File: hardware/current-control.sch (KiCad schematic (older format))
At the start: 9 parts, among them J201 Conn_01x01_Male, Q201 BTS141, U102 TLV4333, U201 DAC6571

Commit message: After footprint check, before layout
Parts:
- added R201, R206: 10K, Resistor_SMD:R_0805_2012Metric_Pad1.15x1.40mm_HandSolder, symbol Device:R
- added R207: 22K, Resistor_SMD:R_0805_2012Metric_Pad1.15x1.40mm_HandSolder, symbol Device:R
- added R208: 220K, Resistor_SMD:R_0805_2012Metric_Pad1.15x1.40mm_HandSolder, symbol Device:R
- C201: MPN (none) -> 885012207098
- J201: MPN (none) -> RA-T2X-64E
- R202: renamed from R201; value 23K -> 220K; MPN (none) -> CRGP0805F220K
- R203: renamed from R202; value 10K -> 22K; MPN (none) -> CRGP0805F22K
- R204: renamed from R203; MPN (none) -> CRGP0805F1K0
- R205: renamed from R204; value 0.1, 1W -> 10m, 3W; MPN SR3R1000FE66 -> RMCJ2U00R01FS
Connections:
- net GND: now also R201.2, R206.2, R207.2
- net I_SENSE: now also R208.1; no longer U102.6 (-)
- net at R202.2, R203.1, U102.3 (+): now also R201.1
- new net: R206.1, R207.1, R208.2, U102.6 (-)
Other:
- note added: "0-0.1V"
- note added: "0.01Ω sense resistor => 1A current / 10mV of programming voltage\n\nSo max. programming voltage of 0.1V =>max. current 10A\n\nBTS141 max. I_D = 25 A\n\nI = 10A, R = 0.01Ω => Power = I^2 R = 1W\nUse 3W sense resistor to give margin"
- note added: "Amplification of 33 here gives full range\nADC input for sense voltage range of 0-0.1V."
- note removed: "0-1V"
- note removed: "0.1Ω sense resistor => 1A current / 100mV of programming voltage\n\nSo max. programming voltage of 1V =>max. current 10A\n\nBTS141 max. I_D = 25 A"
- moved on the sheet: R203
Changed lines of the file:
@@
 L Device:R R?
 U 1 1 5E5F12A4
-P 5100 3625
+P 5175 3625
 AR Path="/5E5F12A4" Ref="R?"  Part="1"
-AR Path="/5E5EBC79/5E5F12A4" Ref="R202"  Part="1"
-F 0 "R202" H 5170 3671 50  0000 L CNN
-F 1 "10K" H 5170 3580 50  0000 L CNN
-F 2 "Resistor_SMD:R_0805_2012Metric_Pad1.15x1.40mm_HandSolder" V 5030 3625 50  0001 C CNN
-F 3 "~" H 5100 3625 50  0001 C CNN
-	1    5100 3625
+AR Path="/5E5EBC79/5E5F12A4" Ref="R203"  Part="1"
+F 0 "R203" H 5245 3671 50  0000 L CNN
+F 1 "22K" H 5245 3580 50  0000 L CNN
+F 2 "Resistor_SMD:R_0805_2012Metric_Pad1.15x1.40mm_HandSolder" V 5105 3625 50  0001 C CNN
+F 3 "https://www.mouser.at/datasheet/2/418/NG_DS_9-1773463-9_A-1358566.pdf" H 5175 3625 50  0001 C CNN
+F 4 "CRGP0805F22K" H 5175 3625 50  0001 C CNN "MPN"
+	1    5175 3625
 	1    0    0    -1
 $EndComp
@@
 P 7025 4100
 AR Path="/5E5F12B6" Ref="R?"  Part="1"
-AR Path="/5E5EBC79/5E5F12B6" Ref="R204"  Part="1"
-F 0 "R204" H 7095 4146 50  0000 L CNN
-F 1 "0.1, 1W" H 7095 4055 50  0000 L CNN
+AR Path="/5E5EBC79/5E5F12B6" Ref="R205"  Part="1"
+F 0 "R205" H 7095 4146 50  0000 L CNN
+F 1 "10m, 3W" H 7095 4055 50  0000 L CNN
 F 2 "teensy-load:Sense_Resistor" V 6955 4100 50  0001 C CNN
-F 3 "https://www.mouser.at/datasheet/2/427/sr-1762146.pdf" H 7025 4100 50  0001 C CNN
-F 4 "SR3R1000FE66" H 7025 4100 50  0001 C CNN "MPN"
+F 3 "https://www.mouser.at/datasheet/2/611/rmc-series-1074317.pdf" H 7025 4100 50  0001 C CNN
+F 4 "RMCJ2U00R01FS" H 7025 4100 50  0001 C CNN "MPN"
 	1    7025 4100
 	1    0    0    -1
@@
 P 6450 3450
 AR Path="/5E5F12DB" Ref="R?"  Part="1"
-AR Path="/5E5EBC79/5E5F12DB" Ref="R203"  Part="1"
-F 0 "R203" V 6243 3450 50  0000 C CNN
+AR Path="/5E5EBC79/5E5F12DB" Ref="R204"  Part="1"
+F 0 "R204" V 6243 3450 50  0000 C CNN
 F 1 "1K" V 6334 3450 50  0000 C CNN
 F 2 "Resistor_SMD:R_0805_2012Metric_Pad1.15x1.40mm_HandSolder" V 6380 3450 50  0001 C CNN
-F 3 "~" H 6450 3450 50  0001 C CNN
+F 3 "https://www.mouser.at/datasheet/2/418/NG_DS_9-1773463-9_A-1358566.pdf" H 6450 3450 50  0001 C CNN
+F 4 "CRGP0805F1K0" H 6450 3450 50  0001 C CNN "MPN"
 	1    6450 3450
 	0    1    1    0
@@
 Text HLabel 8650 2700 2    50   Input ~ 0
 IN+
-Text HLabel 8650 4475 2    50   Input ~ 0
+Text HLabel 8650 5275 2    50   Input ~ 0
 IN-
-Text Notes 6825 5000 0    50   ~ 0
-0.1Ω sense resistor => 1A current / 100mV of programming voltage\n\nSo max. programming voltage of 1V =>max. current 10A\n\nBTS141 max. I_D = 25 A
+Text Notes 6775 6200 0    50   ~ 0
+0.01Ω sense resistor => 1A current / 10mV of programming voltage\n\nSo max. programming voltage of 0.1V =>max. current 10A\n\nBTS141 max. I_D = 25 A\n\nI = 10A, R = 0.01Ω => Power = I^2 R = 1W\nUse 3W sense resistor to give margin
 Text HLabel 3225 2475 0    50   Input ~ 0
 I2C_SCL
@@
 P 5100 3025
 AR Path="/5E61CCF9" Ref="R?"  Part="1"
-AR Path="/5E5EBC79/5E61CCF9" Ref="R201"  Part="1"
-F 0 "R201" H 5170 3071 50  0000 L CNN
-F 1 "23K" H 5170 2980 50  0000 L CNN
+AR Path="/5E5EBC79/5E61CCF9" Ref="R202"  Part="1"
+F 0 "R202" H 5170 3071 50  0000 L CNN
+F 1 "220K" H 5170 2980 50  0000 L CNN
 F 2 "Resistor_SMD:R_0805_2012Metric_Pad1.15x1.40mm_HandSolder" V 5030 3025 50  0001 C CNN
-F 3 "~" H 5100 3025 50  0001 C CNN
+F 3 "https://www.mouser.at/datasheet/2/418/NG_DS_9-1773463-9_A-1358566.pdf" H 5100 3025 50  0001 C CNN
+F 4 "CRGP0805F220K" H 5100 3025 50  0001 C CNN "MPN"
 	1    5100 3025
 	1    0    0    -1
@@
 Wire Wire Line
 	5625 3350 5100 3350
-Connection ~ 5100 3350
-Wire Wire Line
-	5100 3350 5100 3475
 Wire Wire Line
 	5100 2875 5100 2625
@@
 	5100 2625 4625 2625
 Wire Wire Line
-	7025 4250 7025 4475
-Wire Wire Line
-	7025 4475 8650 4475
+	7025 5275 8650 5275
 Wire Wire Line
 	7025 3650 7025 3825
@@
 	5500 3825 7025 3825
 Connection ~ 7025 3825
-Wire Wire Line
-	5100 3775 5100 3900
 Text Notes 4825 2600 0    50   ~ 0
 0-3.3V
 Text Notes 5200 3325 0    50   ~ 0
-0-1V
+0-0.1V
 Wire Wire Line
 	4175 3900 5100 3900
 Wire Wire Line
 	4175 3100 4175 3900
-Connection ~ 5100 3900
 Wire Wire Line
 	5100 3900 5100 4000
@@
 F 1 "0.1U" H 2165 2455 50  0000 L CNN
 F 2 "Capacitor_SMD:C_0805_2012Metric_Pad1.15x1.40mm_HandSolder" H 2088 2350 50  0001 C CNN
-F 3 "~" H 2050 2500 50  0001 C CNN
+F 3 "https://www.mouser.at/datasheet/2/445/885012207098-1727748.pdf" H 2050 2500 50  0001 C CNN
+F 4 "885012207098" H 2050 2500 50  0001 C CNN "MPN"
 	1    2050 2500
 	1    0    0    -1
@@
 Wire Wire Line
 	8300 4000 8375 4000
-Wire Wire Line
-	8375 4000 8375 4300
-Wire Wire Line
-	8375 4300 7600 4300
-Wire Wire Line
-	7600 4300 7600 4100
 Wire Wire Line
 	7600 4100 7700 4100
@@
 F 1 "Conn_01x01_Male" H 7808 3265 50  0000 C CNN
 F 2 "teensy-load:HeatSink_RA_T2X_64E" H 7700 3175 50  0001 C CNN
-F 3 "~" H 7700 3175 50  0001 C CNN
+F 3 "https://www.ohmite.com/assets/docs/sink_f_r.pdf" H 7700 3175 50  0001 C CNN
+F 4 "RA-T2X-64E" H 7700 3175 50  0001 C CNN "MPN"
 	1    7700 3175
 	1    0    0    -1
@@
 Text Notes 7625 3300 0    50   ~ 0
 Heat sink
+Text Notes 7825 5000 0    50   ~ 0
+Amplification of 33 here gives full range\nADC input for sense voltage range of 0-0.1V.
+$Comp
+L Device:R R208
+U 1 1 5E7C1E35
+P 8075 4400
+F 0 "R208" V 8175 4400 50  0000 C CNN
+F 1 "220K" V 8275 4400 50  0000 C CNN
+F 2 "Resistor_SMD:R_0805_2012Metric_Pad1.15x1.40mm_HandSolder" V 8005 4400 50  0001 C CNN
+F 3 "https://www.mouser.at/datasheet/2/418/NG_DS_9-1773463-9_A-1358566.pdf" H 8075 4400 50  0001 C CNN
+F 4 "CRGP0805F220K" H 8075 4400 50  0001 C CNN "MPN"
+	1    8075 4400
+	0    1    1    0
+$EndComp
+Wire Wire Line
+	7600 4100 7600 4400
+Wire Wire Line
+	8375 4000 8375 4400
+$Comp
+L power:GND #PWR?
+U 1 1 5E7C4D35
+P 7600 4950
+AR Path="/5E7C4D35" Ref="#PWR?"  Part="1"
+AR Path="/5E5EBC79/5E7C4D35" Ref="#PWR0205"  Part="1"
+F 0 "#PWR0205" H 7600 4700 50  0001 C CNN
+F 1 "GND" H 7605 4777 50  0000 C CNN
+F 2 "" H 7600 4950 50  0001 C CNN
+F 3 "" H 7600 4950 50  0001 C CNN
+	1    7600 4950
+	1    0    0    -1
+$EndComp
+Wire Wire Line
+	7025 4250 7025 5275
+$Comp
+L Device:R R?
+U 1 1 5E7D5DFF
+P 5025 3625
+AR Path="/5E7D5DFF" Ref="R?"  Part="1"
+AR Path="/5E5EBC79/5E7D5DFF" Ref="R201"  Part="1"
+F 0 "R201" H 4775 3675 50  0000 L CNN
+F 1 "10K" H 4775 3575 50  0000 L CNN
+F 2 "Resistor_SMD:R_0805_2012Metric_Pad1.15x1.40mm_HandSolder" V 4955 3625 50  0001 C CNN
+F 3 "https://www.mouser.at/datasheet/2/418/NG_DS_9-1773463-9_A-1358566.pdf" H 5025 3625 50  0001 C CNN
+F 4 "CRGP0805F1K0" H 5025 3625 50  0001 C CNN "MPN"
+	1    5025 3625
+	1    0    0    -1
+$EndComp
+Wire Wire Line
+	5175 3450 5100 3450
+Wire Wire Line
+	5100 3450 5025 3450
+Connection ~ 5100 3450
+Wire Wire Line
+	5025 3800 5100 3800
+Connection ~ 5100 3800
+Wire Wire Line
+	5100 3800 5175 3800
+Wire Wire Line
+	5025 3800 5025 3775
+Wire Wire Line
+	5175 3800 5175 3775
+Wire Wire Line
+	5100 3800 5100 3900
+Connection ~ 5100 3900
+Wire Wire Line
+	5100 3350 5100 3450
+Connection ~ 5100 3350
+Wire Wire Line
+	5025 3450 5025 3475
+Wire Wire Line
+	5175 3450 5175 3475
+$Comp
+L Device:R R?
+U 1 1 5E7EBF3C
+P 7675 4675
+AR Path="/5E7EBF3C" Ref="R?"  Part="1"
+AR Path="/5E5EBC79/5E7EBF3C" Ref="R207"  Part="1"
+F 0 "R207" H 7745 4721 50  0000 L CNN
+F 1 "22K" H 7745 4630 50  0000 L CNN
+F 2 "Resistor_SMD:R_0805_2012Metric_Pad1.15x1.40mm_HandSolder" V 7605 4675 50  0001 C CNN
+F 3 "https://www.mouser.at/datasheet/2/418/NG_DS_9-1773463-9_A-1358566.pdf" H 7675 4675 50  0001 C CNN
+F 4 "CRGP0805F22K" H 7675 4675 50  0001 C CNN "MPN"
+	1    7675 4675
+	1    0    0    -1
+$EndComp
+$Comp
+L Device:R R?
+U 1 1 5E7EBF43
+P 7525 4675
+AR Path="/5E7EBF43" Ref="R?"  Part="1"
+AR Path="/5E5EBC79/5E7EBF43" Ref="R206"  Part="1"
+F 0 "R206" H 7275 4725 50  0000 L CNN
+F 1 "10K" H 7275 4625 50  0000 L CNN
+F 2 "Resistor_SMD:R_0805_2012Metric_Pad1.15x1.40mm_HandSolder" V 7455 4675 50  0001 C CNN
+F 3 "https://www.mouser.at/datasheet/2/418/NG_DS_9-1773463-9_A-1358566.pdf" H 7525 4675 50  0001 C CNN
+F 4 "CRGP0805F1K0" H 7525 4675 50  0001 C CNN "MPN"
+	1    7525 4675
+	1    0    0    -1
+$EndComp
+Wire Wire Line
+	7675 4500 7600 4500
+Wire Wire Line
+	7600 4500 7525 4500
+Connection ~ 7600 4500
+Wire Wire Line
+	7525 4850 7600 4850
+Connection ~ 7600 4850
+Wire Wire Line
+	7600 4850 7675 4850
+Wire Wire Line
+	7525 4850 7525 4825
+Wire Wire Line
+	7675 4850 7675 4825
+Wire Wire Line
+	7600 4850 7600 4950
+Wire Wire Line
+	7600 4400 7600 4500
+Wire Wire Line
+	7525 4500 7525 4525
+Wire Wire Line
+	7675 4500 7675 4525
+Connection ~ 7600 4400
+Wire Wire Line
+	7600 4400 7925 4400
+Wire Wire Line
+	8225 4400 8375 4400
 $EndSCHEMATC

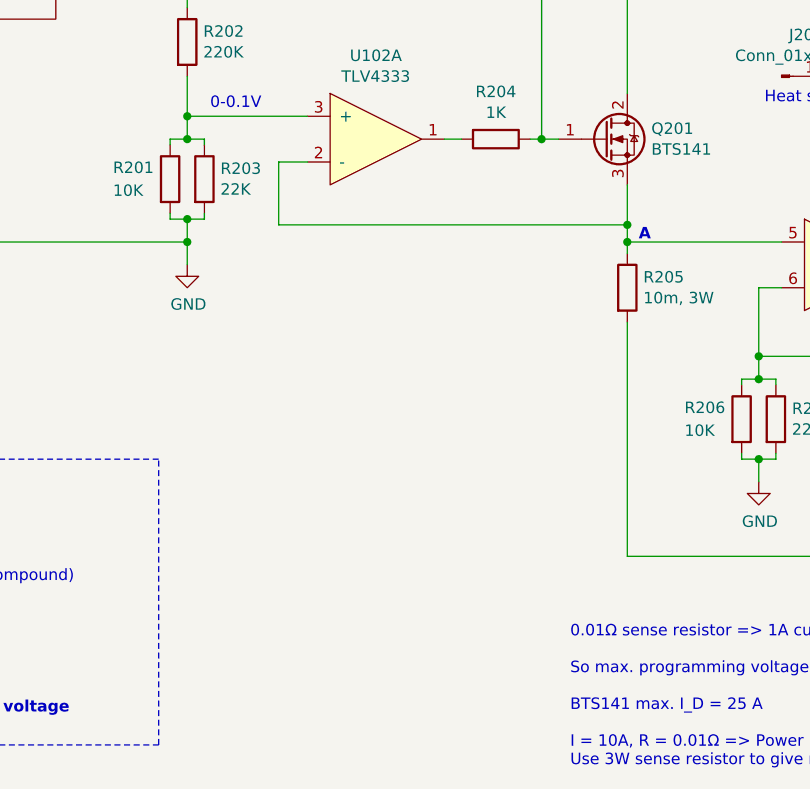
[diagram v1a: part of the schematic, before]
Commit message: Add possible biasing modification to schematic
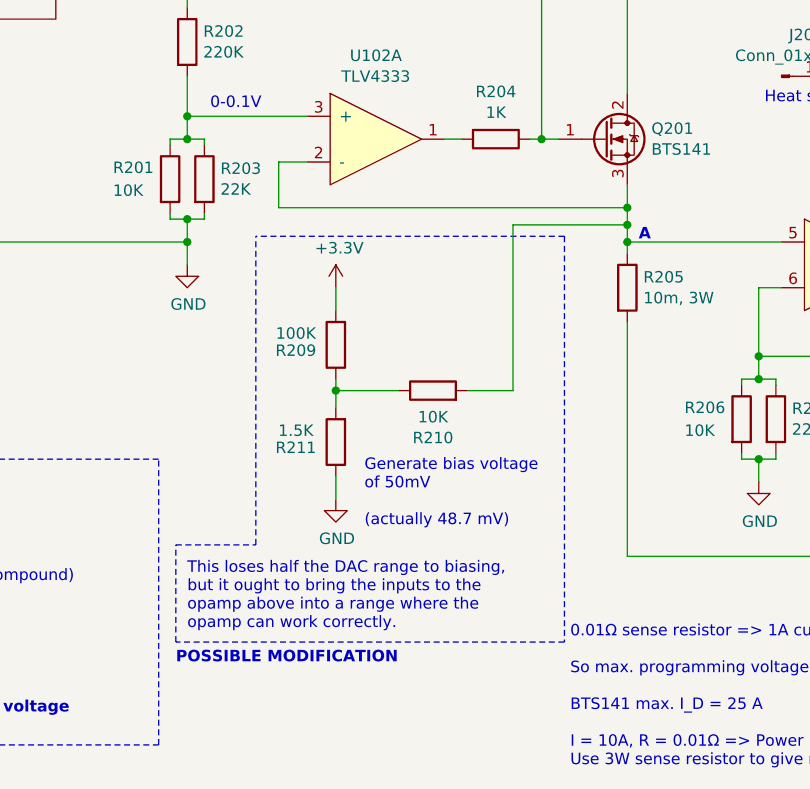
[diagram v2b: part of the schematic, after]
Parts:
- added R209: 100K, Resistor_SMD:R_0805_2012Metric_Pad1.15x1.40mm_HandSolder, symbol Device:R
- added R210: 10K, Resistor_SMD:R_0805_2012Metric_Pad1.15x1.40mm_HandSolder, symbol Device:R
- added R211: 1.5K, Resistor_SMD:R_0805_2012Metric_Pad1.15x1.40mm_HandSolder, symbol Device:R
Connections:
- net +3V3: now also R209.2
- net GND: now also R211.1
- net at Q201.3 (S), R205.1, U102.2 (-)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: now also R210.2
- new net: R209.1, R210.1, R211.2
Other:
- note added: "Generate bias voltage\nof 50mV\n\n(actually 48.7 mV)"
- note added: "POSSIBLE MODIFICATION"
- note added: "This loses half the DAC range to biasing,\nbut it ought to bring the inputs to the\nopamp above into a range where the\nopamp can work correctly."
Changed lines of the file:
@@
 	7025 5275 8650 5275
 Wire Wire Line
-	7025 3650 7025 3825
+	7025 3650 7025 3750
 Wire Wire Line
 	5625 3550 5500 3550
 Wire Wire Line
-	5500 3550 5500 3825
-Wire Wire Line
-	5500 3825 7025 3825
-Connection ~ 7025 3825
+	5500 3550 5500 3750
+Wire Wire Line
+	5500 3750 7025 3750
+Connection ~ 7025 3750
 Text Notes 4825 2600 0    50   ~ 0
 0-3.3V
@@
 	2050 2350 2050 2125
 Wire Wire Line
-	7025 3825 7025 3900
+	7025 3750 7025 3825
 Connection ~ 7025 3900
 Wire Wire Line
@@
 Wire Wire Line
 	8225 4400 8375 4400
+$Comp
+L power:GND #PWR?
+U 1 1 5F10D516
+P 5750 5025
+AR Path="/5F10D516" Ref="#PWR?"  Part="1"
+AR Path="/5E5EBC79/5F10D516" Ref="#PWR02"  Part="1"
+F 0 "#PWR02" H 5750 4775 50  0001 C CNN
+F 1 "GND" H 5755 4852 50  0000 C CNN
+F 2 "" H 5750 5025 50  0001 C CNN
+F 3 "" H 5750 5025 50  0001 C CNN
+	1    5750 5025
+	1    0    0    -1
+$EndComp
+$Comp
+L power:+3.3V #PWR01
+U 1 1 5F10DB53
+P 5750 4100
+F 0 "#PWR01" H 5750 3950 50  0001 C CNN
+F 1 "+3.3V" H 5765 4273 50  0000 C CNN
+F 2 "" H 5750 4100 50  0001 C CNN
+F 3 "" H 5750 4100 50  0001 C CNN
+	1    5750 4100
+	1    0    0    -1
+$EndComp
+Wire Wire Line
+	5750 4100 5750 4200
+Wire Wire Line
+	5750 4500 5750 4550
+Wire Wire Line
+	5750 4925 5750 5025
+Wire Wire Line
+	6025 4550 5750 4550
+Connection ~ 5750 4550
+Wire Wire Line
+	5750 4550 5750 4625
+Wire Wire Line
+	6325 4550 6525 4550
+Wire Wire Line
+	6525 4550 6525 3825
+Wire Wire Line
+	6525 3825 7025 3825
+Connection ~ 7025 3825
+Wire Wire Line
+	7025 3825 7025 3900
+$Comp
+L Device:R R?
+U 1 1 5F10C69E
+P 5750 4350
+AR Path="/5F10C69E" Ref="R?"  Part="1"
+AR Path="/5E5EBC79/5F10C69E" Ref="R209"  Part="1"
+F 0 "R209" H 5925 4375 50  0000 C CNN
+F 1 "100K" H 5925 4300 50  0000 C CNN
+F 2 "Resistor_SMD:R_0805_2012Metric_Pad1.15x1.40mm_HandSolder" V 5680 4350 50  0001 C CNN
+F 3 "https://www.mouser.at/datasheet/2/418/NG_DS_9-1773463-9_A-1358566.pdf" H 5750 4350 50  0001 C CNN
+F 4 "CRGP0805F1K0" H 5750 4350 50  0001 C CNN "MPN"
+	1    5750 4350
+	-1   0    0    1
+$EndComp
+$Comp
+L Device:R R?
+U 1 1 5F10CB4F
+P 5750 4775
+AR Path="/5F10CB4F" Ref="R?"  Part="1"
+AR Path="/5E5EBC79/5F10CB4F" Ref="R211"  Part="1"
+F 0 "R211" H 5925 4800 50  0000 C CNN
+F 1 "1.5K" H 5925 4725 50  0000 C CNN
+F 2 "Resistor_SMD:R_0805_2012Metric_Pad1.15x1.40mm_HandSolder" V 5680 4775 50  0001 C CNN
+F 3 "https://www.mouser.at/datasheet/2/418/NG_DS_9-1773463-9_A-1358566.pdf" H 5750 4775 50  0001 C CNN
+F 4 "CRGP0805F1K0" H 5750 4775 50  0001 C CNN "MPN"
+	1    5750 4775
+	-1   0    0    1
+$EndComp
+$Comp
+L Device:R R?
+U 1 1 5F10CFCE
+P 6175 4550
+AR Path="/5F10CFCE" Ref="R?"  Part="1"
+AR Path="/5E5EBC79/5F10CFCE" Ref="R210"  Part="1"
+F 0 "R210" V 5968 4550 50  0000 C CNN
+F 1 "10K" V 6059 4550 50  0000 C CNN
+F 2 "Resistor_SMD:R_0805_2012Metric_Pad1.15x1.40mm_HandSolder" V 6105 4550 50  0001 C CNN
+F 3 "https://www.mouser.at/datasheet/2/418/NG_DS_9-1773463-9_A-1358566.pdf" H 6175 4550 50  0001 C CNN
+F 4 "CRGP0805F1K0" H 6175 4550 50  0001 C CNN "MPN"
+	1    6175 4550
+	0    -1   -1   0
+$EndComp
+Text Notes 5875 5150 0    50   ~ 0
+Generate bias voltage\nof 50mV\n\n(actually 48.7 mV)
+Text Notes 5100 5600 0    50   ~ 0
+This loses half the DAC range to biasing,\nbut it ought to bring the inputs to the\nopamp above into a range where the\nopamp can work correctly.
+Wire Notes Line
+	6750 5650 5050 5650
+Wire Notes Line
+	5050 5650 5050 5225
+Wire Notes Line
+	5050 5225 5400 5225
+Wire Notes Line
+	5400 5225 5400 3875
+Text Notes 5050 5750 0    50   ~ 10
+POSSIBLE MODIFICATION
+Wire Notes Line
+	6750 3875 6750 5650
+Wire Notes Line
+	6750 3875 5400 3875
 $EndSCHEMATC

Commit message: Start of revision 2 design changes
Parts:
- removed J201: Conn_01x01_Male, teensy-load:HeatSink_RA_T2X_64E, symbol Connector:Conn_01x01_Male
- removed R209: 100K, Resistor_SMD:R_0805_2012Metric_Pad1.15x1.40mm_HandSolder, symbol Device:R
- removed R210: 10K, Resistor_SMD:R_0805_2012Metric_Pad1.15x1.40mm_HandSolder, symbol Device:R
- removed R211: 1.5K, Resistor_SMD:R_0805_2012Metric_Pad1.15x1.40mm_HandSolder, symbol Device:R
- removed U102: TLV4333, Package_SO:SOIC-14_3.9x8.7mm_P1.27mm, symbol teensy-load:TLV4333
- added C202, C203: 0.1U, Capacitor_SMD:C_0805_2012Metric_Pad1.15x1.40mm_HandSolder, symbol Device:C
- added HS201: Heatsink, teensy-load:HeatSink_RA_T2X_64E, symbol Mechanical:Heatsink
- added U202, U203: TLV333IDBVR, Package_TO_SOT_SMD:SOT-23-5, symbol teensy-load:TLV333IDBVR
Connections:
- net +3V3: now also C202.1, C203.1, U202.5 (V+), U203.5 (V+)
- net GND: now also C202.2, C203.2, U202.2 (V-), U203.2 (V-)
- net I_SENSE: now also U203.1
- net at R201.1, R202.2, R203.1: now also U202.3 (+)
- net at Q201.3 (S), R205.1: now also U202.4 (-), U203.3 (+)
- net at R204.2: now also U202.1
- net at R206.1, R207.1, R208.2: now also U203.4 (-)
- no-connect marks 1 -> 0
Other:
- note removed: "Heat sink"
- moved on the sheet: R205, R206, R207, R208
